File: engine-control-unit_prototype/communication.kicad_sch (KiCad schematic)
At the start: 38 parts, among them J10 I2C, J11 CANFD, J12 ADXL345, J13 MAG_CONN_1, J14 MAG_CONN_2, J15 JTAG, J16 USB_C_Receptacle_USB2.0_man, Q1 PMOS, U8 TCAN337G, U9 USBLC6-2SC6

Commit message: VDD_3V3 is now VDD_3V6 (Removed LDO) LEDs now have the right symbol (oops x2)
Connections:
- net VDD_3V3 renamed VDD_3V6
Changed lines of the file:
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@@
 			)
 		)
-		(property "Value" "VDD_3V3"
+		(property "Value" "VDD_3V6"
 			(at 219.71 100.33 0)
 			(effects
@@
 			)
 		)
-		(property "Value" "VDD_3V3"
+		(property "Value" "VDD_3V6"
 			(at 99.06 31.75 0)
 			(effects
@@
 			)
 		)
-		(property "Value" "VDD_3V3"
+		(property "Value" "VDD_3V6"
 			(at 59.69 36.83 0)
 			(effects
@@
 			)
 		)
-		(property "Value" "VDD_3V3"
+		(property "Value" "VDD_3V6"
 			(at 50.8 77.47 0)
 			(effects
@@
 			)
 		)
-		(property "Value" "VDD_3V3"
+		(property "Value" "VDD_3V6"
 			(at 184.15 129.54 0)
 			(effects
@@
 			)
 		)
-		(property "Value" "VDD_3V3"
+		(property "Value" "VDD_3V6"
 			(at 205.74 43.18 0)
 			(effects
@@
 			)
 		)
-		(property "Value" "VDD_3V3"
+		(property "Value" "VDD_3V6"
 			(at 212.09 69.85 0)
 			(effects
@@
 			)
 		)
-		(property "Value" "VDD_3V3"
+		(property "Value" "VDD_3V6"
 			(at 224.79 25.4 0)
 			(effects

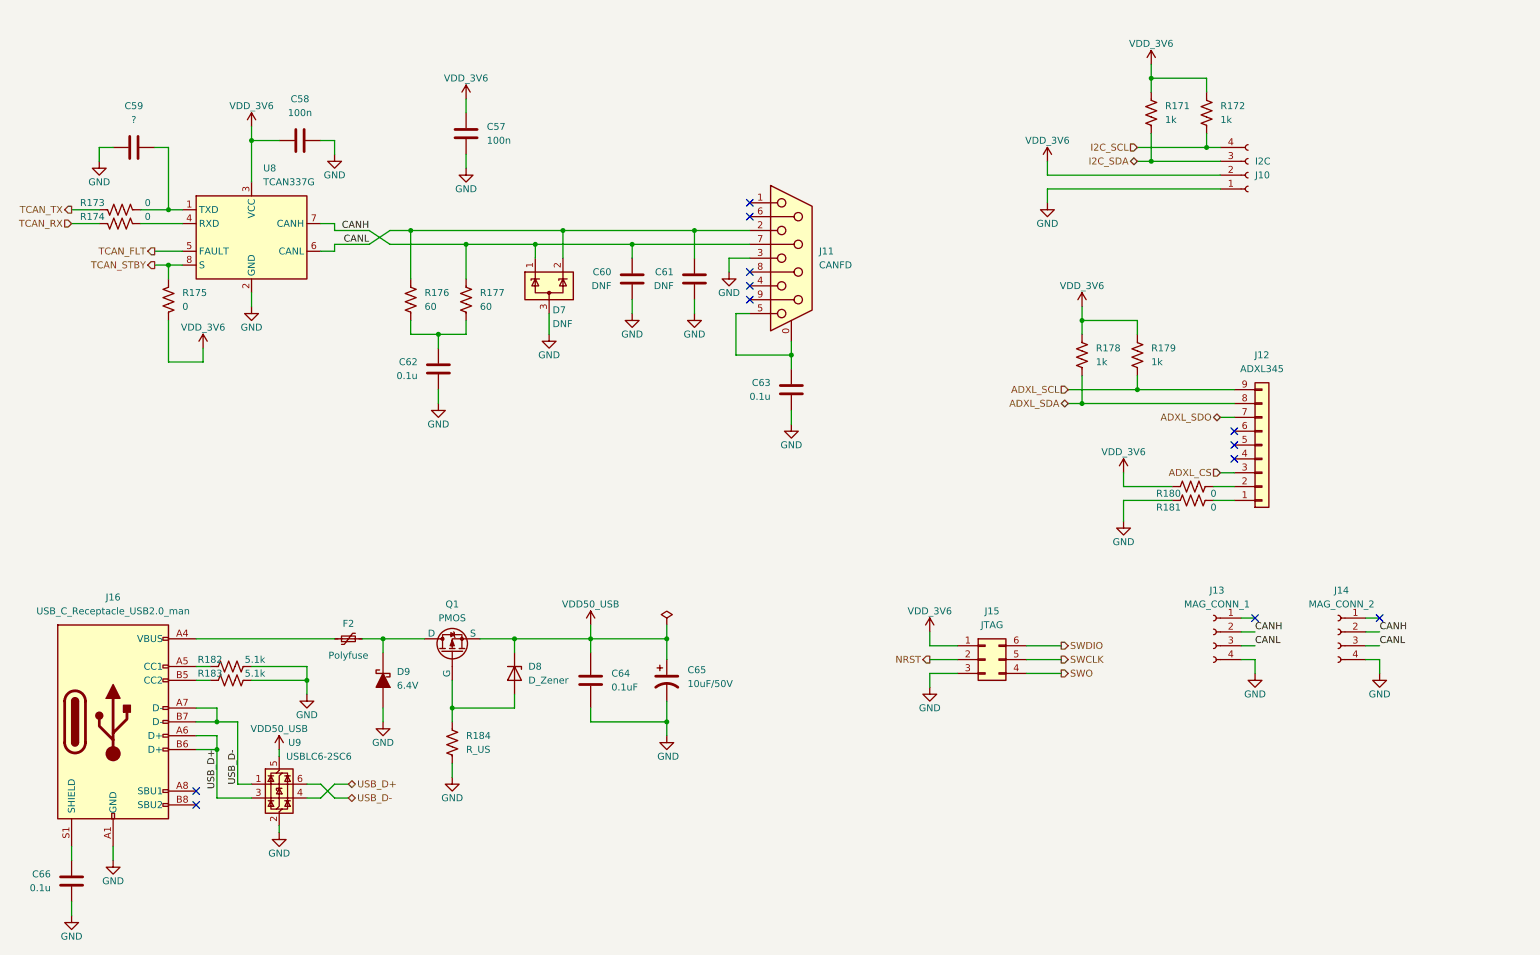
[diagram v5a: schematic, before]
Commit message: Started layout Added some footprints
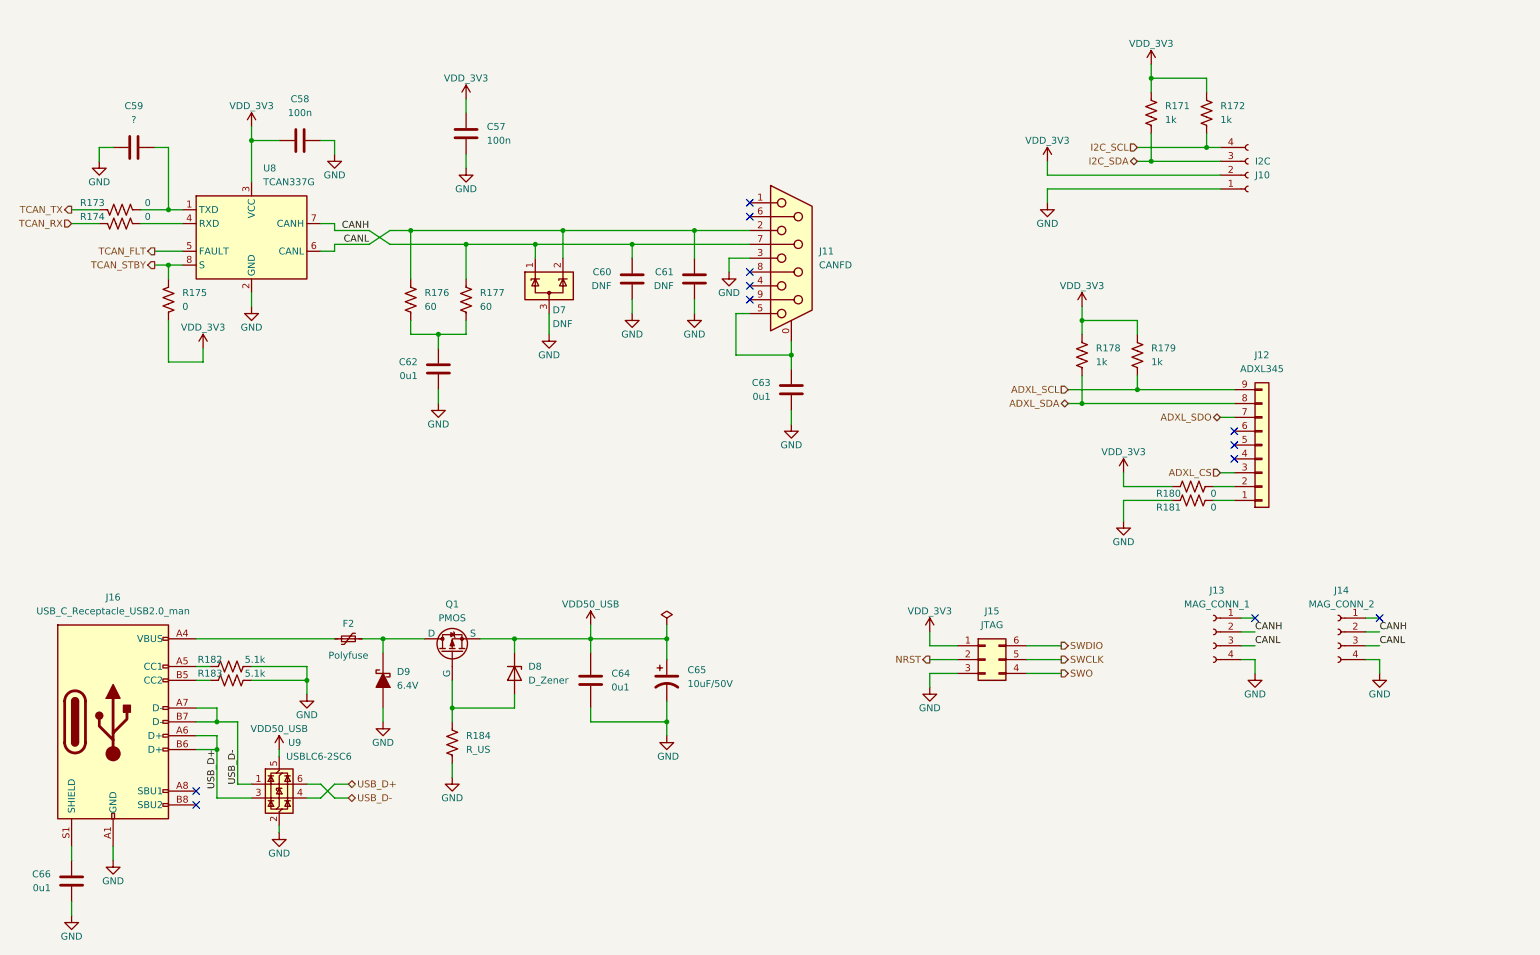
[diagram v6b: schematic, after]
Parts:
- C57, C58, C59, C60, C61: footprint Capacitor_SMD:C_0603_1608Metric -> Capacitor_SMD:C_0402_1005Metric
- C62, C63, C66: value 0.1u -> 0u1; footprint Capacitor_SMD:C_0603_1608Metric -> Capacitor_SMD:C_0402_1005Metric
- C64: value 0.1uF -> 0u1; footprint Capacitor_SMD:C_0603_1608Metric -> Capacitor_SMD:C_0402_1005Metric
- J10, J13, J14: footprint (none) -> Connector_PinSocket_2.54mm:PinSocket_1x04_P2.54mm_Vertical
- J11: footprint (none) -> Connector_Dsub:DSUB-9_Pins_Horizontal_P2.77x2.84mm_EdgePinOffset7.70mm_Housed_MountingHolesOffset9.12mm
- J12: footprint (none) -> Connector_PinSocket_2.54mm:PinSocket_1x09_P2.54mm_Vertical
- U8: footprint (none) -> Package_SO:SOIC-8_3.9x4.9mm_P1.27mm
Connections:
- net VDD_3V6 renamed VDD_3V3
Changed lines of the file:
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@@
 			)
 		)
-		(property "Value" "0.1u"
+		(property "Value" "0u1"
 			(at 154.94 90.1699 0)
 			(effects
@@
 			)
 		)
-		(property "Footprint" "Capacitor_SMD:C_0603_1608Metric"
+		(property "Footprint" "Capacitor_SMD:C_0402_1005Metric"
 			(at 159.7152 85.09 0)
 			(effects
@@
 			)
 		)
-		(property "Footprint" "Capacitor_SMD:C_0603_1608Metric"
+		(property "Footprint" "Capacitor_SMD:C_0402_1005Metric"
 			(at 98.0948 38.1 0)
 			(effects
@@
 			)
 		)
-		(property "Footprint" "Capacitor_SMD:C_0603_1608Metric"
+		(property "Footprint" "Capacitor_SMD:C_0402_1005Metric"
 			(at 141.9352 64.77 0)
 			(effects
@@
 			)
 		)
-		(property "Value" "VDD_3V6"
+		(property "Value" "VDD_3V3"
 			(at 219.71 100.33 0)
 			(effects
@@
 			)
 		)
-		(property "Footprint" ""
+		(property "Footprint" "Package_SO:SOIC-8_3.9x4.9mm_P1.27mm"
 			(at 59.69 73.66 0)
 			(effects
@@
 			)
 		)
-		(property "Footprint" "Capacitor_SMD:C_0603_1608Metric"
+		(property "Footprint" "Capacitor_SMD:C_0402_1005Metric"
 			(at 41.91 43.4848 0)
 			(effects
@@
 			)
 		)
-		(property "Value" "VDD_3V6"
+		(property "Value" "VDD_3V3"
 			(at 99.06 31.75 0)
 			(effects
@@
 			)
 		)
-		(property "Value" "VDD_3V6"
+		(property "Value" "VDD_3V3"
 			(at 59.69 36.83 0)
 			(effects
@@
 			)
 		)
-		(property "Footprint" ""
+		(property "Footprint" "Connector_PinSocket_2.54mm:PinSocket_1x09_P2.54mm_Vertical"
 			(at 245.11 99.06 0)
 			(effects
@@
 			)
 		)
-		(property "Footprint" "Capacitor_SMD:C_0603_1608Metric"
+		(property "Footprint" "Capacitor_SMD:C_0402_1005Metric"
 			(at 130.5052 64.77 0)
 			(effects
@@
 			)
 		)
-		(property "Value" "VDD_3V6"
+		(property "Value" "VDD_3V3"
 			(at 50.8 77.47 0)
 			(effects
@@
 			)
 		)
-		(property "Value" "VDD_3V6"
+		(property "Value" "VDD_3V3"
 			(at 184.15 129.54 0)
 			(effects
@@
 			)
 		)
-		(property "Value" "0.1u"
+		(property "Value" "0u1"
 			(at 22.86 180.3399 0)
 			(effects
@@
 			)
 		)
-		(property "Footprint" "Capacitor_SMD:C_0603_1608Metric"
+		(property "Footprint" "Capacitor_SMD:C_0402_1005Metric"
 			(at 27.6352 175.26 0)
 			(effects
@@
 			)
 		)
-		(property "Footprint" ""
+		(property "Footprint" "Connector_PinSocket_2.54mm:PinSocket_1x04_P2.54mm_Vertical"
 			(at 259.08 133.35 0)
 			(effects
@@
 			)
 		)
-		(property "Footprint" "Capacitor_SMD:C_0603_1608Metric"
+		(property "Footprint" "Capacitor_SMD:C_0402_1005Metric"
 			(at 72.39 42.2148 0)
 			(effects
@@
 			)
 		)
-		(property "Footprint" ""
+		(property "Footprint" "Connector_PinSocket_2.54mm:PinSocket_1x04_P2.54mm_Vertical"
 			(at 236.22 133.35 0)
 			(effects
@@
 			)
 		)
-		(property "Value" "0.1uF"
+		(property "Value" "0u1"
 			(at 125.73 143.5099 0)
 			(effects
@@
 			)
 		)
-		(property "Footprint" "Capacitor_SMD:C_0603_1608Metric"
+		(property "Footprint" "Capacitor_SMD:C_0402_1005Metric"
 			(at 121.92 124.46 0)
 			(effects
@@
 			)
 		)
-		(property "Footprint" ""
+		(property "Footprint" "Connector_PinSocket_2.54mm:PinSocket_1x04_P2.54mm_Vertical"
 			(at 242.57 49.53 0)
 			(effects
@@
 			)
 		)
-		(property "Value" "VDD_3V6"
+		(property "Value" "VDD_3V3"
 			(at 205.74 43.18 0)
 			(effects
@@
 			)
 		)
-		(property "Footprint" ""
+		(property "Footprint" "Connector_Dsub:DSUB-9_Pins_Horizontal_P2.77x2.84mm_EdgePinOffset7.70mm_Housed_MountingHolesOffset9.12mm"
 			(at 158.75 64.77 0)
 			(effects
@@
 			)
 		)
-		(property "Value" "VDD_3V6"
+		(property "Value" "VDD_3V3"
 			(at 212.09 69.85 0)
 			(effects
@@
 			)
 		)
-		(property "Value" "0.1u"
+		(property "Value" "0u1"
 			(at 90.17 86.3599 0)
 			(effects
@@
 			)
 		)
-		(property "Footprint" "Capacitor_SMD:C_0603_1608Metric"
+		(property "Footprint" "Capacitor_SMD:C_0402_1005Metric"
 			(at 94.9452 81.28 0)
 			(effects
@@
 			)
 		)
-		(property "Value" "VDD_3V6"
+		(property "Value" "VDD_3V3"
 			(at 224.79 25.4 0)
 			(effects

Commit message: Added better LIB tree Continued PCB layout Some fixes Added chip for protection
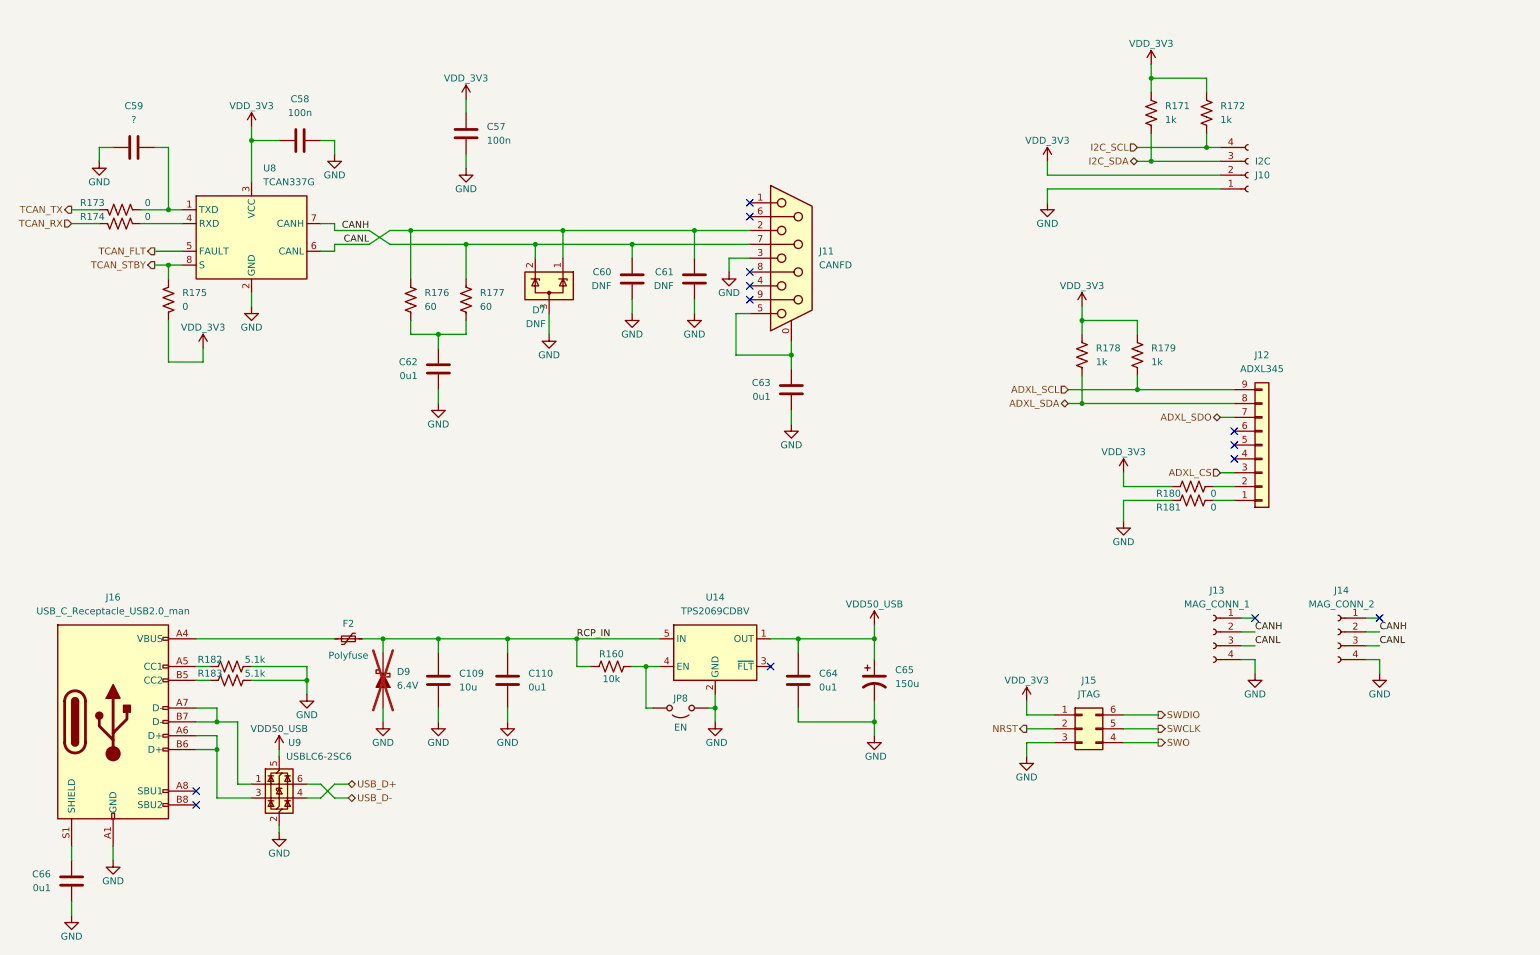
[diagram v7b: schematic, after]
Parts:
- removed D8: D_Zener, symbol Device:D_Zener
- removed Q1: PMOS, symbol Simulation_SPICE:PMOS
- removed R184: R_US, Resistor_SMD:R_0603_1608Metric, symbol Device:R_US
- added C109: 10u, Capacitor_SMD:C_0603_1608Metric, symbol 0CSL_D1_V1:CAP_7mm_X_2mm
- added C110: 0u1, Capacitor_SMD:C_0402_1005Metric, symbol 0CSL_D1_V1:CAP_7mm_X_2mm
- added JP8: EN, Jumper:SolderJumper-2_P1.3mm_Open_RoundedPad1.0x1.5mm, symbol Jumper:Jumper_2_Open
- added R160: 10k, Resistor_SMD:R_0603_1608Metric, symbol Device:R_US
- added U14: TPS2069CDBV, Package_TO_SOT_SMD:SOT-23-5, symbol Power_Management:TPS2069CDBV
- C65: value 10uF/50V -> 150u; footprint (none) -> Capacitor_Tantalum_SMD:CP_EIA-7343-31_Kemet-D
- D9: now not fitted
- R182, R183: footprint Resistor_SMD:R_0603_1608Metric -> Resistor_SMD:R_0402_1005Metric
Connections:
- net CANH: now also D7.2 (K); no longer D7.1 (K)
- net CANL: now also D7.1 (K); no longer D7.2 (K)
- net GND: now also C109.2, C110.2, JP8.1 (A), U14.2 (GND)
- net USB_D+: no longer J16.A6 (D+), J16.B6 (D+), U9.3 (I/O2)
- net USB_D-: no longer J16.A7 (D-), J16.B7 (D-), U9.1 (I/O1)
- net VDD50_USB: now also U14.1 (OUT)
- net RCP_IN: now reaches D9.1 (K), F2.2
- net RCP_IN: now also C109.1, C110.1, R160.1, U14.5 (IN)
- new net: JP8.2 (B), R160.2, U14.4 (EN)
- new net: J16.A7 (D-), J16.B7 (D-), U9.1 (I/O1)
- new net: J16.A6 (D+), J16.B6 (D+), U9.3 (I/O2)
- no-connect marks 12 -> 13
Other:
- moved on the sheet: C64, C65, J15

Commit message: Continued layout
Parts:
- removed J10: I2C, Connector_PinSocket_2.54mm:PinSocket_1x04_P2.54mm_Vertical, symbol Connector:Conn_01x04_Socket
- removed R171, R172: 1k, Resistor_SMD:R_0402_1005Metric, symbol Device:R_US
- J11: footprint Connector_Dsub:DSUB-9_Pins_Horizontal_P2.77x2.84mm_EdgePinOffset7.70mm_Housed_MountingHolesOffset9.12mm -> Connector_Dsub:DSUB-9_Socket_Vertical_P2.77x2.84mm_MountingHoles
